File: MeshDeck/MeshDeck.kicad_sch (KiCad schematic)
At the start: 34 parts, among them CN1 ATGM336H-6N-74, SW1 4*4*1.7, U1 ESP32-S3-WROOM-1(N16R8), U2 SX1262S8S+T-X1, U3 TPS6282533DMQR, U4 BQ24074RGTR

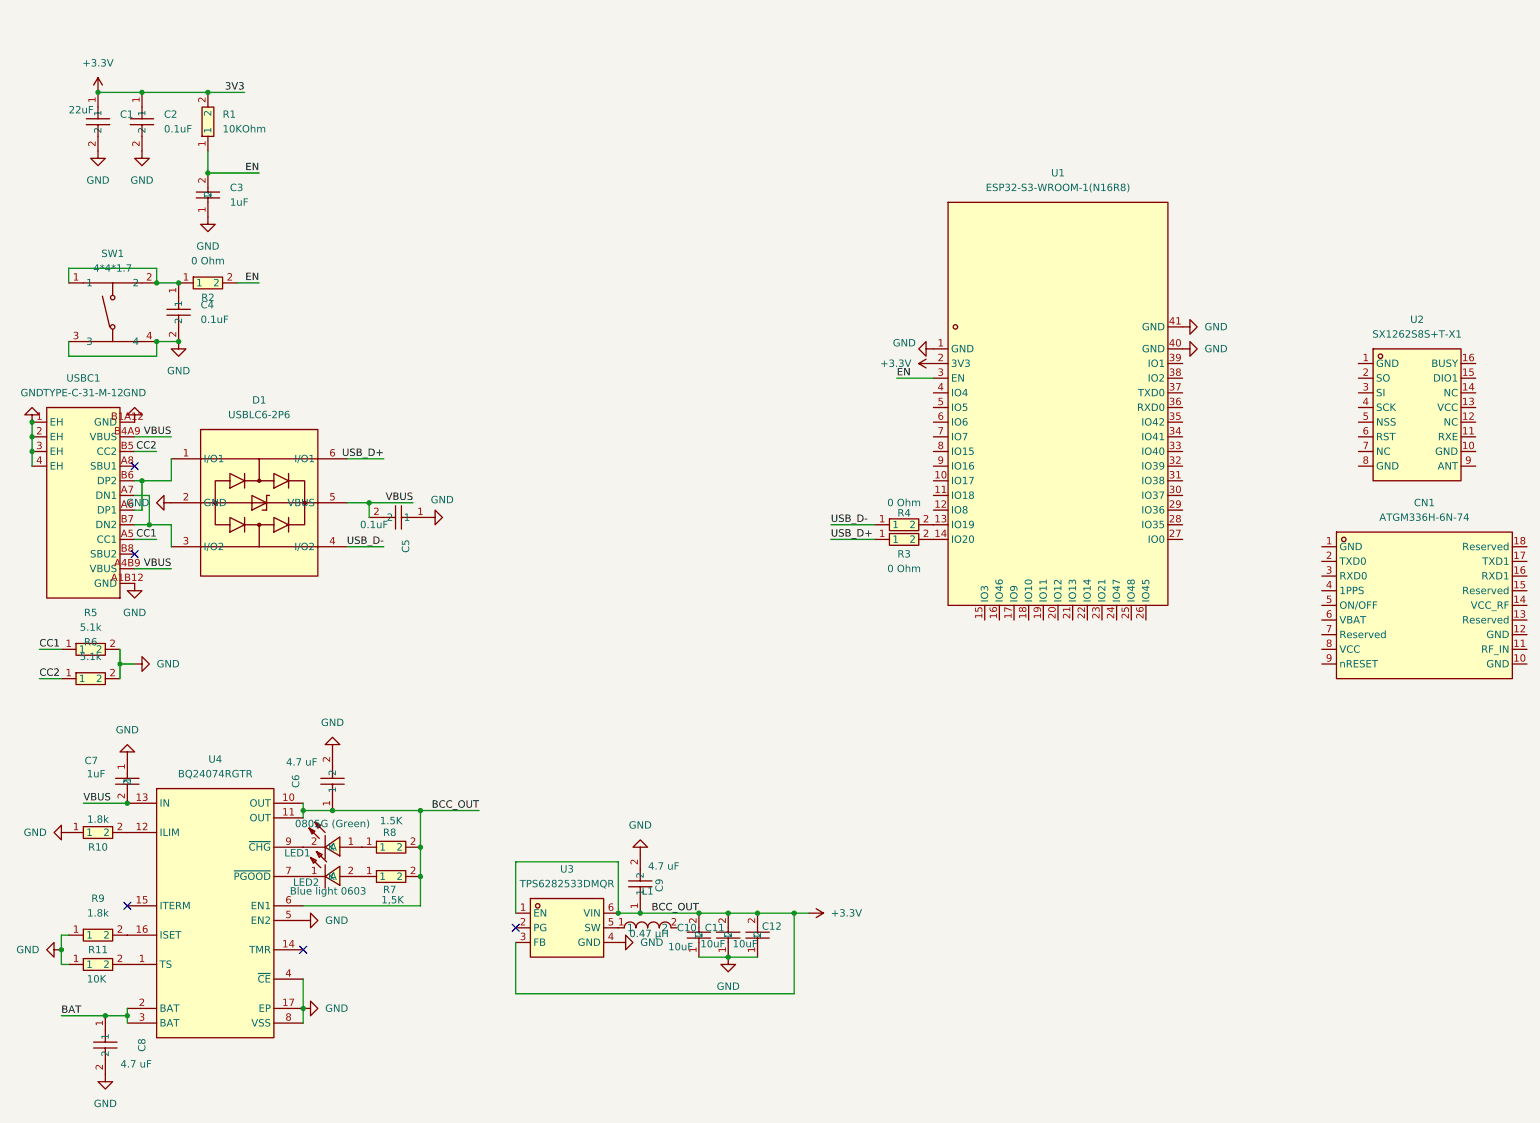
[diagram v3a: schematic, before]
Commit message: Added oscillator, tidied up with subsheets and added boot btn
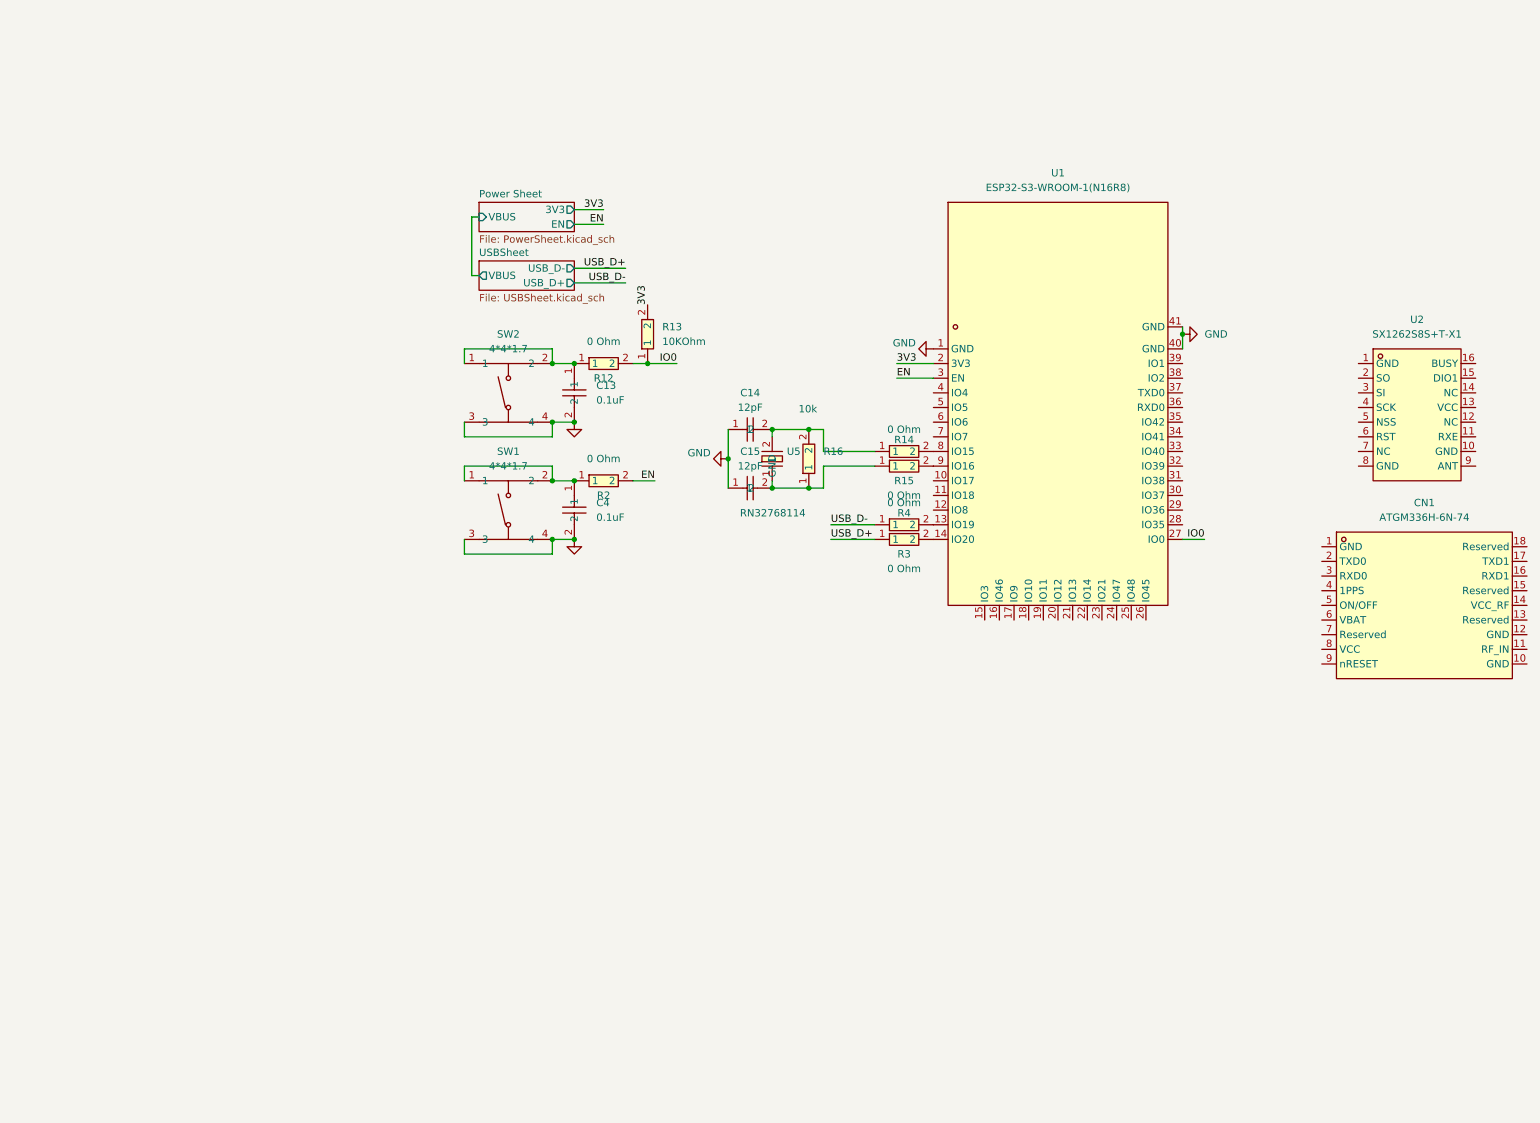
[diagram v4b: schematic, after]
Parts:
- removed C1: 22uF, MeshDeck:C0402, symbol MeshDeck:CL05A226MQ5QUNC
- removed C10, C11, C12: 10uF, MeshDeck:C0402, symbol MeshDeck:CL05A106MQ5NUNC
- removed C2, C5: 0.1uF, MeshDeck:C0402, symbol MeshDeck:CL05B104KO5NNNC
- removed C3, C7: 1uF, MeshDeck:C0402, symbol MeshDeck:CL05A105KP5NNNC
- removed C6, C8, C9: 4.7 uF, MeshDeck:C0402, symbol MeshDeck:CL05A475MP5NRNC
- removed D1: USBLC6-2P6, MeshDeck:SOT-666-6_L1.6-W1.2-P0.50-LS1.6-BR, symbol MeshDeck:USBLC6-2P6
- removed L1: 0.47 µH, MeshDeck:L0402, symbol MeshDeck:LSCNB1005EETR47MB
- removed LED1: 0805G (Green), MeshDeck:LED0805-R-RD, symbol MeshDeck:0805G(Green)
- removed LED2: Blue light 0603, MeshDeck:LED0603-RD, symbol MeshDeck:Bluelight0603
- removed R1: 10KOhm, MeshDeck:R0402, symbol MeshDeck:QR0402F1KQ10
- removed R10, R9: 1.8k, MeshDeck:R0402, symbol MeshDeck:0402WGF1801TCE
- removed R11: 10K, MeshDeck:R0402, symbol MeshDeck:0402WGF1002TCE
- removed R5, R6: 5.1k, MeshDeck:R0402, symbol MeshDeck:0402WGF5101TCE
- removed R7: 1,5K, MeshDeck:R0402, symbol MeshDeck:CR0402JF01R5G
- removed R8: 1.5K, MeshDeck:R0402, symbol MeshDeck:CR0402JF01R5G
- removed U3: TPS6282533DMQR, MeshDeck:VSON-6_L1.5-W1.5-P0.50-TL, symbol MeshDeck:TPS6282533DMQR
- removed U4: BQ24074RGTR, MeshDeck:QFN-16_L3.0-W3.0-P0.50-TL-EP1.7, symbol MeshDeck:BQ24074RGTR
- removed USBC1: TYPE-C-31-M-12, MeshDeck:USB-C_SMD-TYPE-C-31-M-12_1, symbol MeshDeck:TYPE-C-31-M-12
- added C13: 0.1uF, MeshDeck:C0402, symbol MeshDeck:CL05B104KO5NNNC
- added C14, C15: 12pF, MeshDeck:C0402, symbol MeshDeck:0402CG120J500NT
- added R12, R14, R15: 0 Ohm, MeshDeck:R0402, symbol MeshDeck:0402WGF0000TCE
- added R13: 10KOhm, MeshDeck:R0402, symbol MeshDeck:QR0402F1KQ10
- added R16: 10k, MeshDeck:R0402, symbol MeshDeck:0402WGF1002TCE
- added SW2: 4*4*1.7, MeshDeck:SW-SMD_4P-L5.2-W5.2-P3.70-LS6.5, symbol MeshDeck:4*4*1.7
- added U5: RN32768114, MeshDeck:OSC-TH_BD2.0-P0.50, symbol MeshDeck:RN32768114
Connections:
- net GND: now also C13.2, C14.1, C15.1, SW2.3, SW2.4
- net IO0: now reaches U1.27 (IO0)
- net IO0: now also R12.2, R13.1
- net at U1.8 (IO15): now also R14.2
- net at U1.9 (IO16): now also R15.2
- net +3.3V renamed 3V3
- net 3V3: now also R13.2
- new net: C15.2, R15.1, R16.1, U5.1
- new net: C13.1, R12.1, SW2.1, SW2.2
- new net: C14.2, R14.1, R16.2, U5.2 (GND)
- no-connect marks 5 -> 0
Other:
- added sheet Power Sheet (PowerSheet.kicad_sch)
- added sheet USBSheet (USBSheet.kicad_sch)
- moved on the sheet: C4, R2, SW1

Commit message: set up LoRa module and screen (wip)
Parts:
- added C16: 1uF, MeshDeck:C0402, symbol MeshDeck:CL05A105KP5NNNC
- added C17: 1Nf, MeshDeck:C0402, symbol MeshDeck:0402B102K500NT
- added RF1: HJ-SMA023, MeshDeck:SMA-SMD_HJ-SMA023, symbol MeshDeck:HJ-SMA023
- added U6: ~, MeshDeck:2.8 SPI LCD TFT ST7789, symbol MeshDeck:2.8_TFT_Touch_Screen
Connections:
- net 3V3: now also U2.13 (VCC), C16.2, C17.2
- net GND: now also U2.1 (GND), U2.10 (GND), U2.8 (GND), C16.1, C17.1, RF1.2 (GND), RF1.3 (GND), RF1.4 (GND), RF1.5 (GND)
- net IO14: now reaches U2.11 (RXE)
- net IO14: now also U1.22 (IO14)
- net IO45: now reaches U2.15 (DIO1)
- net IO45: now also U1.26 (IO45)
- net IO13: now reaches U2.16 (BUSY)
- net IO13: now also U1.21 (IO13)
- net SPI.MISO: now reaches U2.2 (SO)
- net SPI.MISO: now also U1.33 (IO40), U6.9 (MISO)
- net SPI.MOSI: now reaches U2.3 (SI)
- net SPI.MOSI: now also U1.34 (IO41), U6.6 (MOSI)
- net SPI.SCK: now reaches U2.4 (SCK)
- net SPI.SCK: now also U1.32 (IO39), U6.7 (SCK)
- net IO9: now reaches U2.5 (NSS)
- net IO9: now also U1.17 (IO9)
- net IO17: now reaches U2.6 (RST)
- net IO17: now also U1.10 (IO17)
- net at U2.9 (ANT): now also RF1.1 (SIG)
- net IO11: now reaches U1.19 (IO11)
- net IO11: now also U6.5 (DC)
- net IO12: now reaches U1.20 (IO12)
- net IO12: now also U6.3 (CS)
- net IO42: now reaches U1.35 (IO42)
- net IO42: now also U6.8 (LED)
- no-connect marks 0 -> 3
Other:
- moved on the sheet: C13, C14, C15, C4, R12, R13, R14, R15, R16, R2, R3, R4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

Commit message: Finished screen
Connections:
- net 3V3: now also U6.1 (VCC)
- net GND: now also U6.2 (GND)
- net SPI.MISO: now also U6.13 (T_MISO)
- net SPI.MOSI: now also U6.12 (T_MOSI)
- net SPI.SCK: now also U6.10 (T_CLK)
- net IO10: now reaches U1.18 (IO10)
- net IO10: now also U6.4 (RESET)
- net IO21: now reaches U1.23 (IO21)
- net IO21: now also U6.11 (T_CS)
- net IO47: now reaches U1.24 (IO47)
- net IO47: now also U6.14 (T_IRQ)
- no-connect marks 3 -> 7

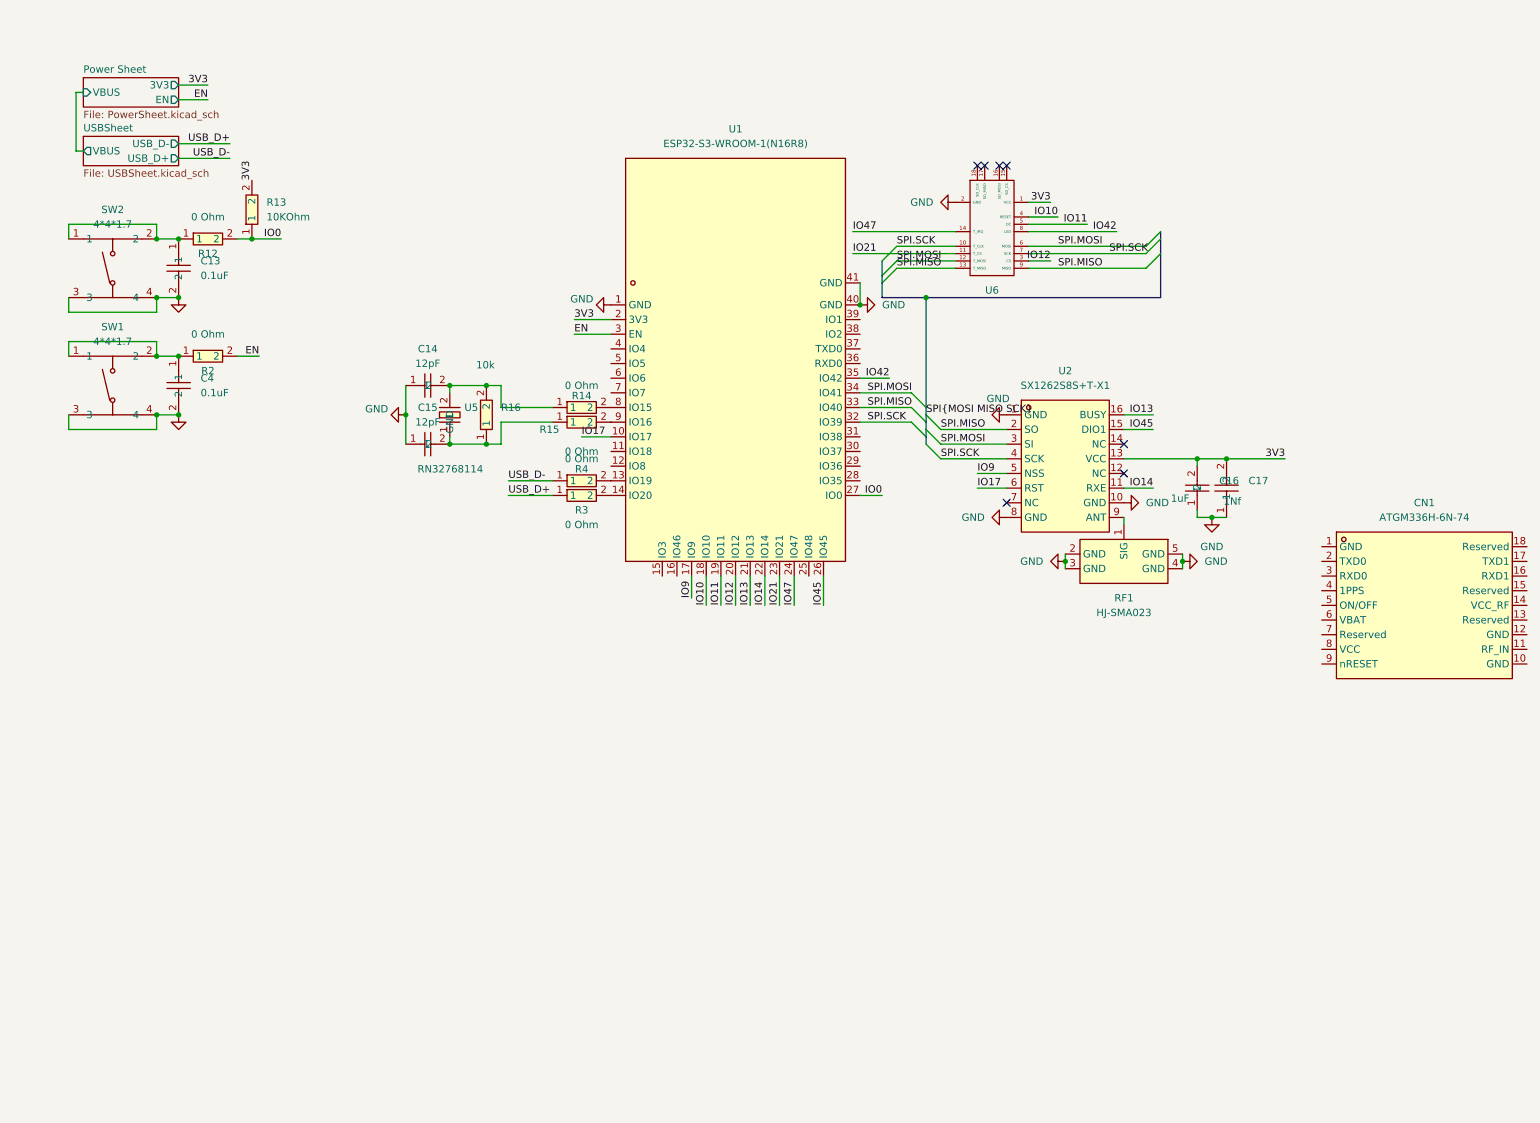
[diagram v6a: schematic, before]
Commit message: Added GPS and sof power button
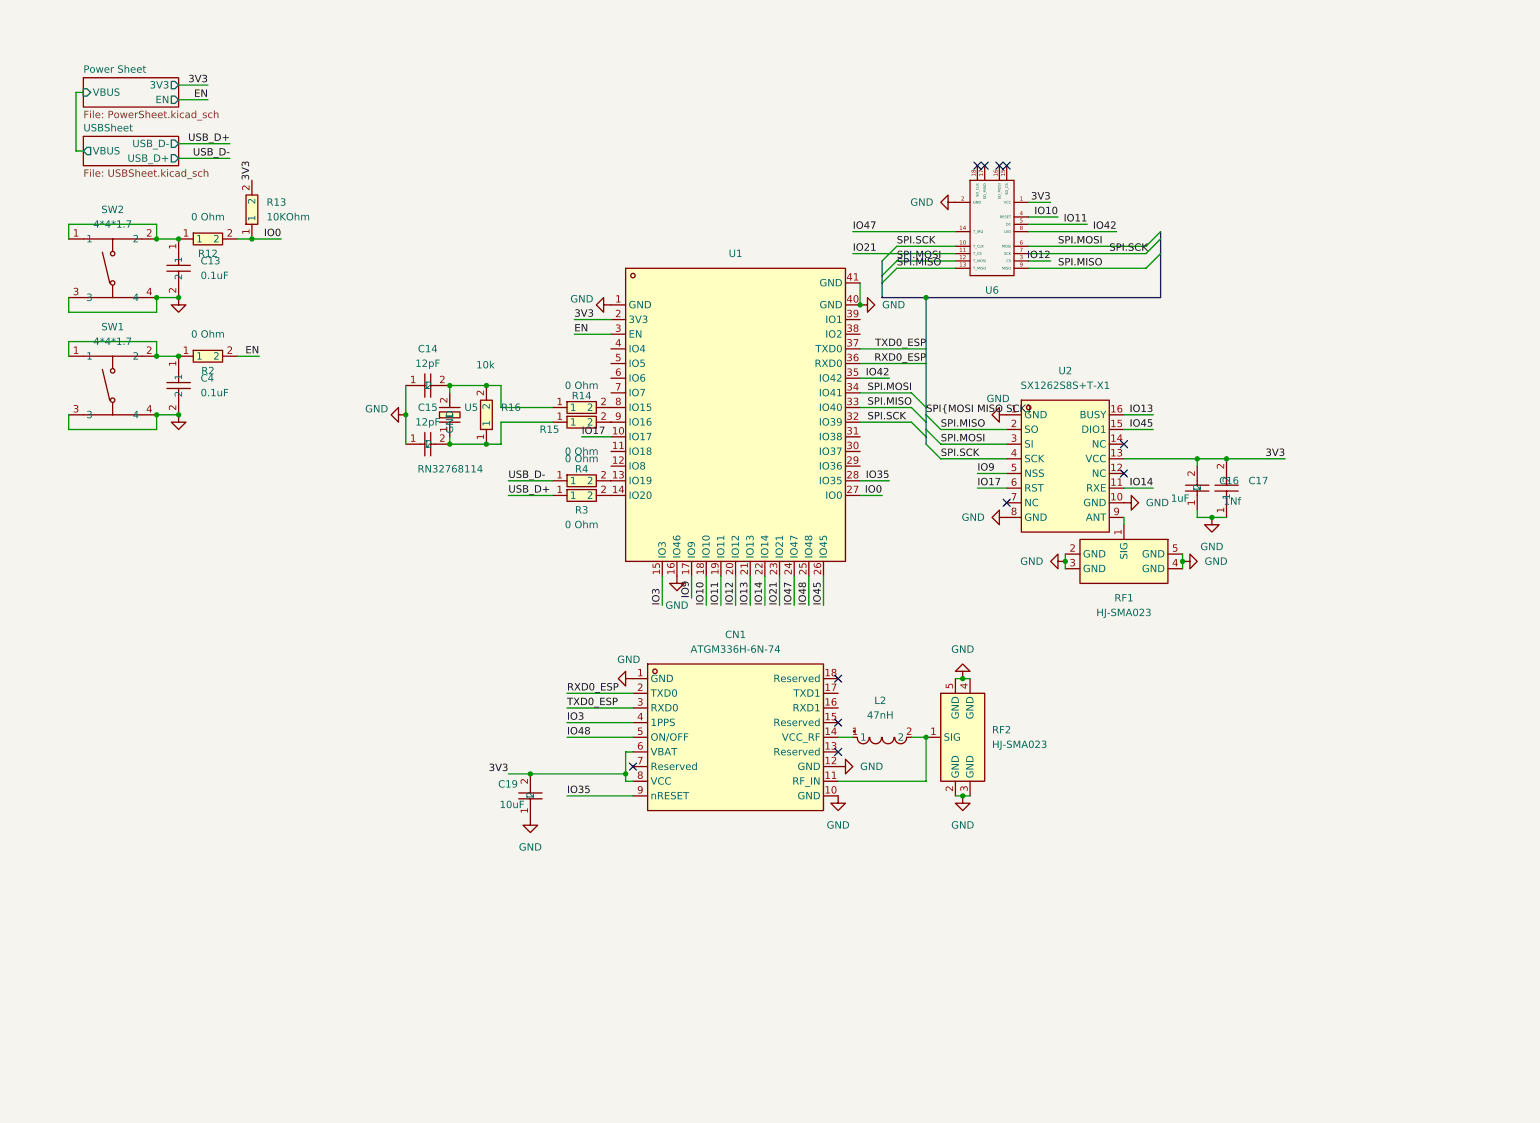
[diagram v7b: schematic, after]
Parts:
- removed U1: ESP32-S3-WROOM-1(N16R8), MeshDeck:WIRELM-SMD_ESP32-S3-WROOM-1, symbol MeshDeck:ESP32-S3-WROOM-1(N16R8)
- added C19: 10uF, MeshDeck:C0402, symbol MeshDeck:CL05A106MQ5NUNC
- added L2: 47nH, MeshDeck:L0402-RD, symbol MeshDeck:LQG15HH47NG02D
- added RF2: HJ-SMA023, MeshDeck:SMA-SMD_HJ-SMA023, symbol MeshDeck:HJ-SMA023
- added U1: ESP32-S3-WROOM-1U-N16R8, MeshDeck:WIRELM-SMD_ESP32-S3-WROOM-1U, symbol MeshDeck:ESP32-S3-WROOM-1U-N16R8
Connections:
- net 3V3: now also CN1.6 (VBAT), CN1.8 (VCC), C19.2, U1.2 (3V3)
- net EN: now also U1.3 (EN)
- net GND: now also CN1.1 (GND), CN1.10 (GND), CN1.12 (GND), C19.1, RF2.2 (GND), RF2.3 (GND), RF2.4 (GND), RF2.5 (GND), U1.1 (GND), U1.16 (IO46), U1.40 (GND), U1.41 (GND)
- net IO0: now also U1.27 (IO0)
- net IO10: now also U1.18 (IO10)
- net IO11: now also U1.19 (IO11)
- net IO12: now also U1.20 (IO12)
- net IO13: now also U1.21 (IO13)
- net IO14: now also U1.22 (IO14)
- net IO17: now also U1.10 (IO17)
- net IO21: now also U1.23 (IO21)
- net IO42: now also U1.35 (IO42)
- net IO45: now also U1.26 (IO45)
- net IO47: now also U1.24 (IO47)
- net IO9: now also U1.17 (IO9)
- net SPI.MISO: now also U1.33 (IO40)
- net SPI.MOSI: now also U1.34 (IO41)
- net SPI.SCK: now also U1.32 (IO39)
- net at R3.2: now also U1.14 (IO20)
- net at R4.2: now also U1.13 (IO19)
- net at CN1.11 (RF_IN): now also L2.2, RF2.1 (SIG)
- net at CN1.14 (VCC_RF): now also L2.1
- net RXD0_ESP: now reaches CN1.2 (TXD0)
- net RXD0_ESP: now also U1.36 (RXD0)
- net TXD0_ESP: now reaches CN1.3 (RXD0)
- net TXD0_ESP: now also U1.37 (TXD0)
- net IO3: now reaches CN1.4 (1PPS)
- net IO3: now also U1.15 (IO3)
- net IO48: now reaches CN1.5 (ON/OFF)
- net IO48: now also U1.25 (IO48)
- net IO35: now reaches CN1.9 (nRESET)
- net IO35: now also U1.28 (IO35)
- net at R14.2: now also U1.8 (IO15)
- net at R15.2: now also U1.9 (IO16)
- no-connect marks 7 -> 11
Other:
- moved on the sheet: CN1
